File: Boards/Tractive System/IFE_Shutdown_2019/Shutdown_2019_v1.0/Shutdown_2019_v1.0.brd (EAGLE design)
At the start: 88.9 x 76.2 mm, 118 parts, among them Q1 DMN6140L-7, Q10 DMN6140L-7, Q11 DMP3099L-7, Q12 IRLML6346PBF, Q13 IRLML6346PBF, Q14 IRLML6346PBF, Q15 DMP3099L-7, Q16 DMN6140L-7, Q17 IRLML6346PBF, Q18 DMN6140L-7, Q2 DMN6140L-7, Q20 DMN6140L-7, Q21 DMN6140L-7, Q3 DMN6140L-7, Q4 DMN6140L-7, Q5 DMN6140L-7, Q6 DMP3099L-7, Q9 DMN6140L-7, U1 STM32F103CBT6, U2 STM32F103CBT6

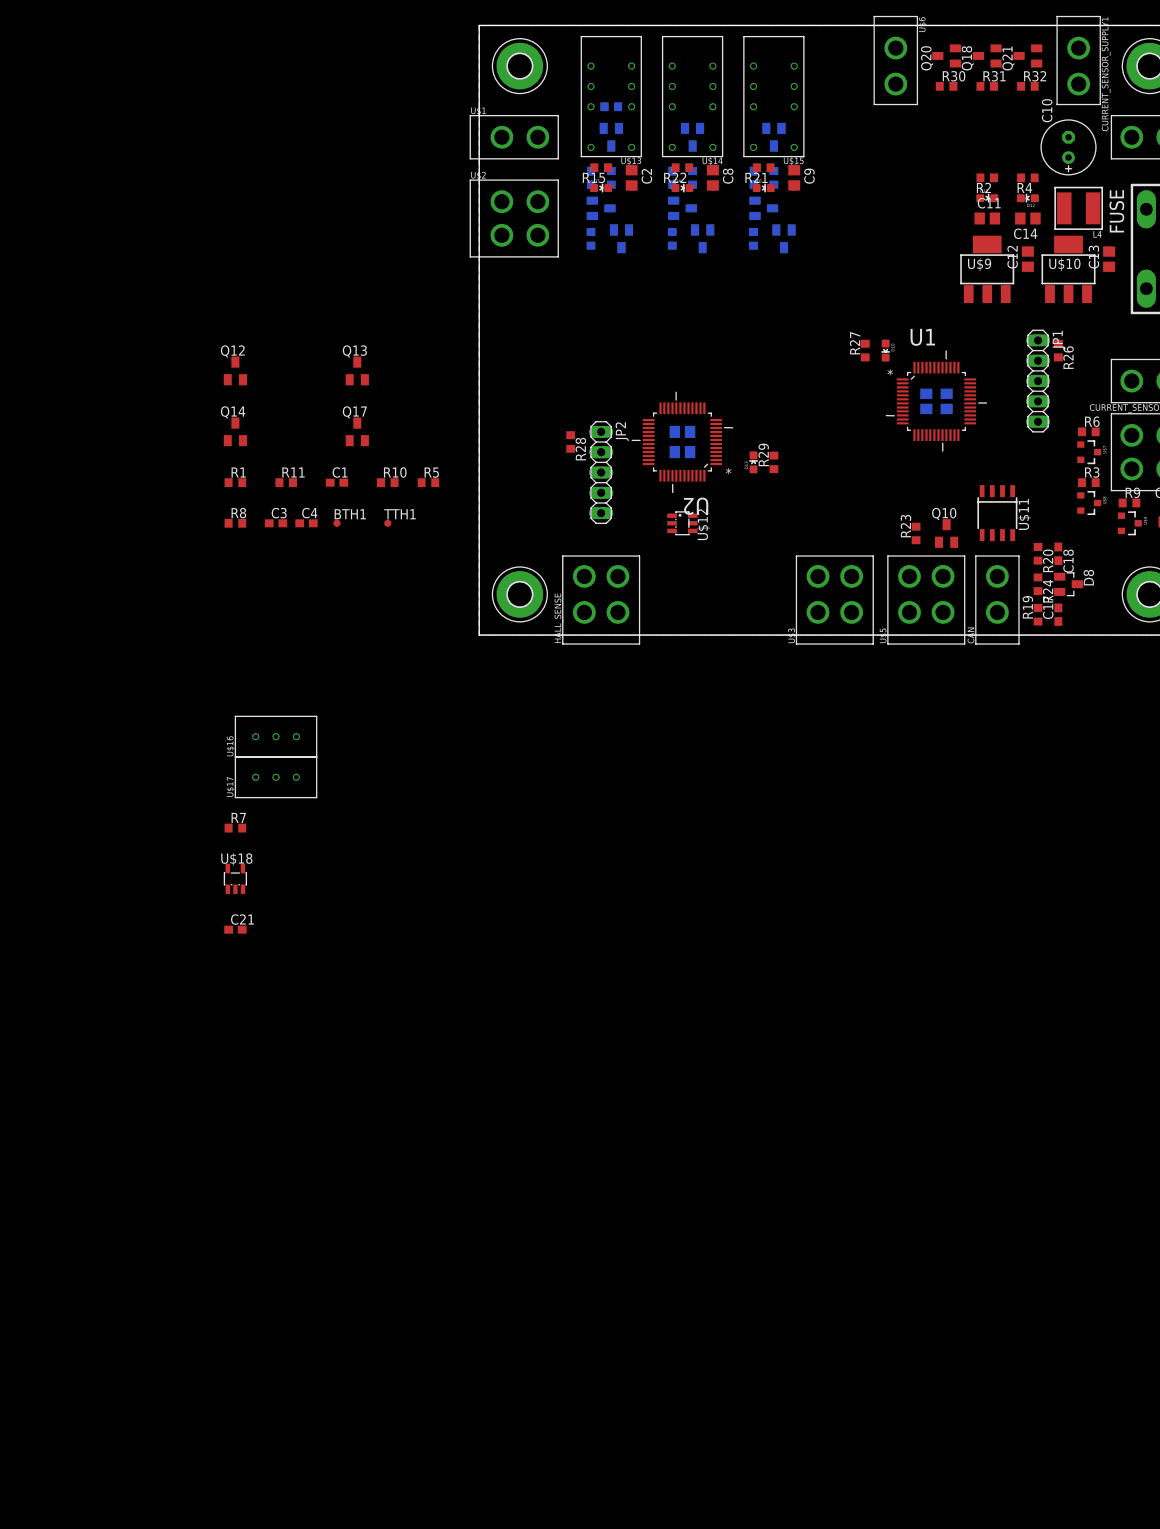
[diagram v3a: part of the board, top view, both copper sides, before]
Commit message: More work, inputs protected with zener and LPF
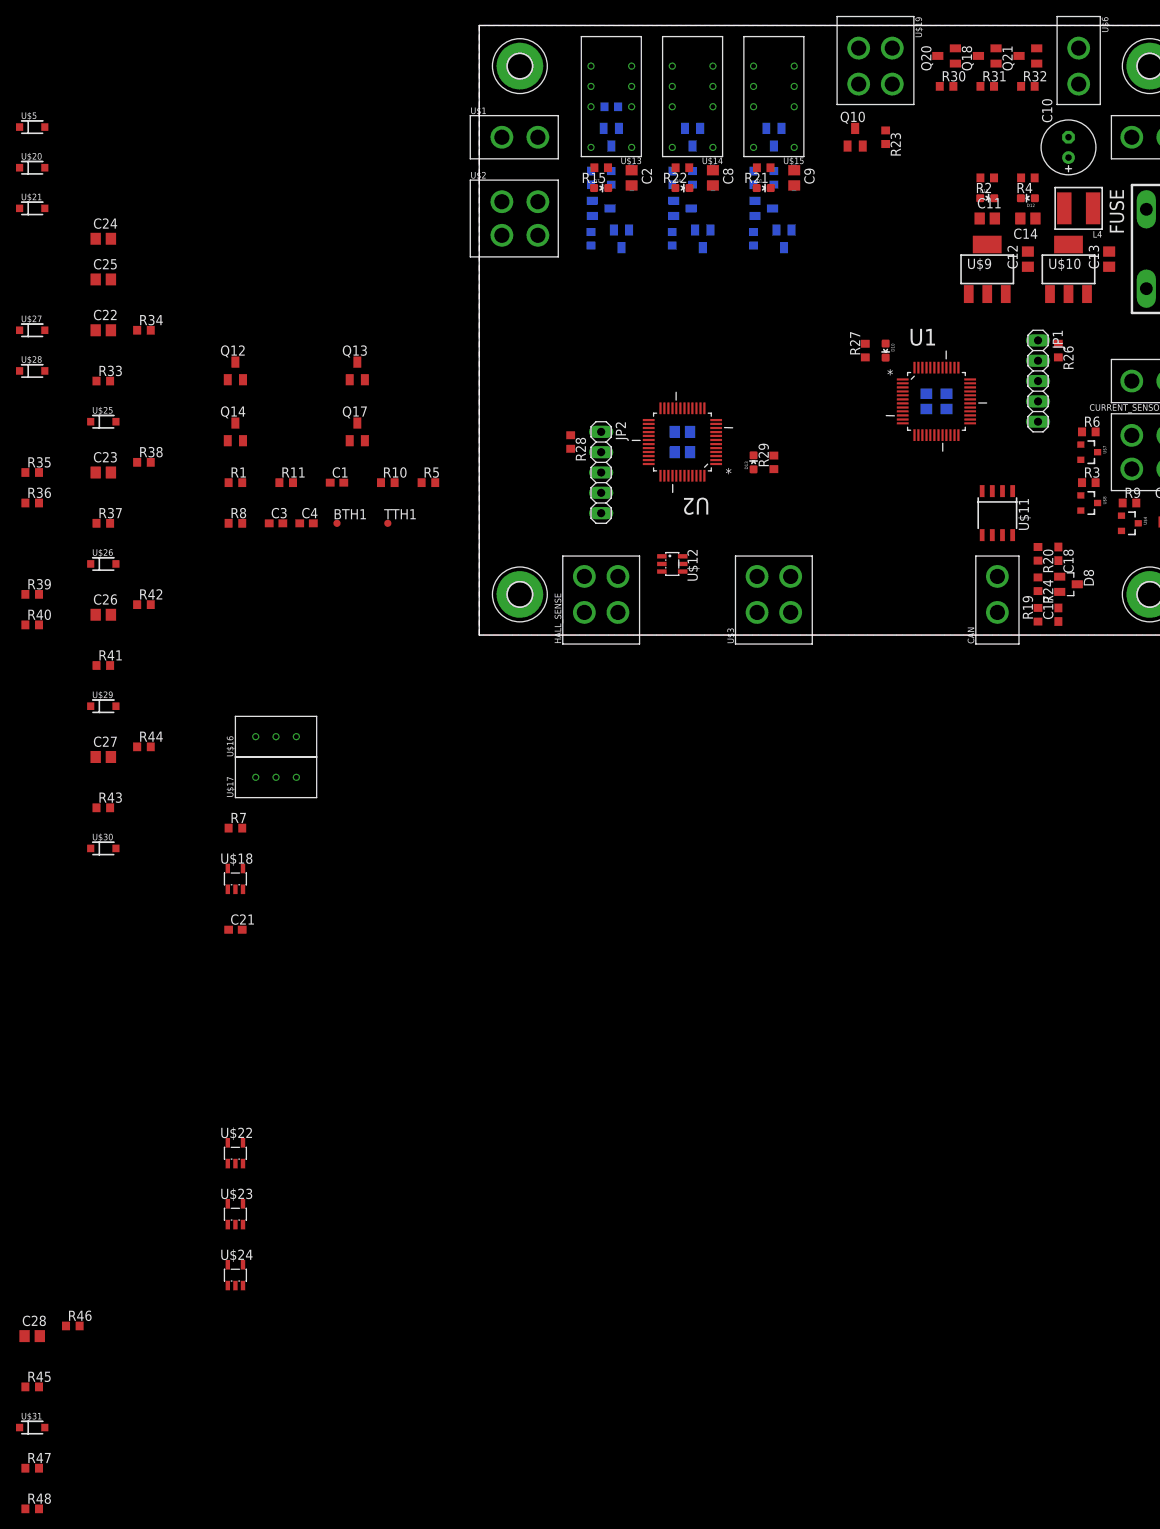
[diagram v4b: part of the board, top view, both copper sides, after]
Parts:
- removed CURRENT_SENSOR_SUPPLY1: MINIFIT_JR_5566-02, Display_Custom:MINIFIT_JR_5566-02
- added C22, C23, C24, C25, C26, C27, C28: 0.1u, rcl:C0805
- added R33, R35, R36, R37, R41, R43, R45: 100, rcl:R0603
- added R34, R38, R39, R40, R42, R44, R46: 100k, rcl:R0603
- added R47, R48: 10k, rcl:R0603
- added U$19: MINIFIT_JR_5566-04, Display_Custom:MINIFIT_JR_5566-04
- added U$20, U$21: BZT52C, DIODES_INC:SOD-123
- added U$22, U$23, U$24: LMV321L, STM:SOT23-5
- added U$25, U$26, U$28, U$29, U$30, U$31: BZT52C13, DIODES_INC:SOD-123
- added U$27: BZT52C5V6, DIODES_INC:SOD-123
- R25: value 10k -> 1k
- U$5: value MINIFIT_JR_5566-04 -> BZT52C; device Display_Custom:MINIFIT_JR_5566-04 -> DIODES_INC:SOD-123
- moved U$5 126.1 mm to (-55.9, 63.5)
- moved Q10 50.8 mm to (47.0, 62.2)
- moved R23 49.7 mm to (50.8, 62.2), turned to 270 degrees
- moved U$6 22.9 mm to (74.9, 71.1)
- moved U$3 7.62 mm to (36.8, 5.08)
- moved U$12 5.24 mm to (24.1, 8.89)
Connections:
- net N$20 renamed THROTTLE_A_F
- removed net REGEN: U$5.3
- removed net WHEEL_ANGLE: U$5.1
- new net FAULT_BMS_F: C23.1, C6.1, Q3.1, R17.2, R38.2
- new net FAULT_BSPD_F: C7.1, Q5.1, R16.2
- new net FAULT_IMD_F: C26.1, C5.1, Q16.1, R18.2, R42.2
- new net FAULT_RESET_F: C22.1, Q11.1, Q15.1, Q6.1, R25.1, R34.2
- new net N$13: R35.2, R39.1, U$27.C
- new net N$26: C24.1, R39.2
- new net N$29: R33.2, R34.1, U$25.C
- new net N$30: C28.1, R46.2
- new net N$33: R35.1
- new net N$36: R45.1
- new net N$37: R37.2, R38.1, U$26.C
- new net N$39: U$22.1
- new net N$40: U$22.3, U$22.4
- new net N$41: U$24.3, U$24.4
- new net N$45: U$24.1
- new net N$46: U$23.1
- new net N$47: U$23.3, U$23.4
- new net N$49: R41.2, R42.1, U$29.C
- new net N$50: R36.2, R40.1, U$28.C
- new net N$51: C25.1, R40.2
- new net N$54: R36.1
- new net N$55: R43.2, R44.1, U$30.C
- new net N$56: C27.1, R44.2
- new net N$57: R43.1
- net +5V: now also R47.1, R48.1, U$19.1, U$22.5, U$23.5, U$24.5; no longer CURRENT_SENSOR_SUPPLY1.1
- net FAULT_BMS: now also R37.1; no longer C6.1, Q3.1, R17.2
- net FAULT_BSPD: no longer C7.1, Q5.1, R16.2
- net FAULT_IMD: now also R41.1; no longer C5.1, Q16.1, R18.2
- net FAULT_RESET: now also R33.1, U$19.4; no longer Q11.1, Q15.1, Q6.1, R25.1, U$5.4
- net GND: now also C22.2, C23.2, C24.2, C25.2, C26.2, C27.2, C28.2, U$19.3, U$22.2, U$23.2, U$24.2, U$25.A, U$26.A, U$27.A, U$28.A, U$29.A, U$30.A, U$31.A
- net HV_CONNECTED: now also U$19.2; no longer CURRENT_SENSOR_SUPPLY1.2
- net N$22: now also R47.2
- net N$23: now also R48.2
- net N$7: now also R45.2, R46.1, U$31.C; no longer Q4.3
- net RTDS-: now also Q4.3

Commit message: Nearly complete... Just BSPD Circuit left
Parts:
- removed C28: 0.1u, rcl:C0805
- removed R46: 100k, rcl:R0603
- removed U$20, U$21, U$5: BZT52C, DIODES_INC:SOD-123
- removed U$31: BZT52C13, DIODES_INC:SOD-123
- added C29, C30, C31, C32: 0.1u, rcl:C0805
- added C33, C34, C35, C36: 0.001u, rcl:C0805
- added R49, R51, R53, R55: 100, rcl:R0603
- added R50, R52, R54, R56: 100k, rcl:R0603
- added R57, R59, R61, R63: 10, rcl:R0603
- added R58, R60, R62, R64: 10k, rcl:R0603
- added R65, R66, R67, R68: 1k, rcl:R0603
- added U$32, U$33, U$34, U$35, U$36, U$37, U$38, U$39: BZT52C5V6, DIODES_INC:SOD-123
- R45: value 100 -> 10k
- moved R45 146.1 mm to (-55.9, -240.0)
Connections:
- net N$41 renamed BRAKE_PRESSURE_F
- net N$47 renamed THROTTLE_B_F
- removed net HALL_FL_3_3: U2.25
- removed net HALL_FR_3_3: U2.26
- removed net HALL_RL_3_3: U2.27
- removed net HALL_RR_3_3: U2.28
- removed net N$18: U1.30
- removed net N$22: R47.2, U$12.4
- removed net N$23: R48.2, U$12.3
- removed net N$30: C28.1, R46.2
- removed net N$36: R45.1
- removed net N$40: U$22.3, U$22.4
- removed net N$5: U1.29
- removed net N$7: R45.2, R46.1, U$31.C
- removed net REGEN_3_3: U1.11
- new net HALL_FL_F: C33.1, R58.2, U2.25
- new net HALL_FR_F: C34.1, R60.2, U2.26
- new net HALL_RL_F: C35.1, R62.2, U2.27
- new net HALL_RR_F: C36.1, R64.2, U2.28
- new net N$20: R49.2, R50.1, U$32.C
- new net N$38: C29.1, R50.2
- new net N$52: R51.2, R52.1, U$33.C
- new net N$53: C30.1, R52.2
- new net N$59: R53.2, R54.1, U$34.C
- new net N$60: C31.1, R54.2
- new net N$62: R55.2, R56.1, U$35.C
- new net N$63: C32.1, R56.2
- new net N$64: R55.1
- new net N$65: R57.2, R58.1, R65.1, U$36.C
- new net N$68: R59.2, R60.1, R66.1, U$37.C
- new net N$71: R61.2, R62.1, R67.1, U$38.C
- new net N$74: R63.2, R64.1, R68.1, U$39.C
- net +5V: now also R45.2, R65.2, R66.2, R67.2, R68.2
- net BRAKE_PRESSURE: now also R53.1
- net GND: now also C29.2, C30.2, C31.2, C32.2, C33.2, C34.2, C35.2, C36.2, U$32.A, U$33.A, U$34.A, U$35.A, U$36.A, U$37.A, U$38.A, U$39.A; no longer C28.2, U$31.A
- net HALL_FL: now also R57.1
- net HALL_FR: now also R59.1
- net HALL_RL: now also R61.1
- net HALL_RR: now also R63.1
- net SCL_TC: now also R48.2, U$12.3
- net SDA_TC: now also R47.2, U$12.4
- net THROTTLE_A: now also R51.1
- net THROTTLE_A_F: now also U$22.3, U$22.4
- net THROTTLE_B: now also R49.1
- net THROTTLE_OUT: now also R45.1

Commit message: Moving to layout of shutdown
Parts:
- removed U$27, U$35: BZT52C5V6, DIODES_INC:SOD-123
- removed U$28, U$30: BZT52C13, DIODES_INC:SOD-123
- added BRAKE, CURR: PV36, BOURNS:PV36
- added C28: 0.1u, resistor:C0603
- added Q7: DMN6140L-7, TRANS:SOT23
- added R46, R69, R70, R71, R72, R73, R74: 10k, rcl:R0603
- added U$20, U$5: TS881, STM:SOT23-5
- added U$21: BZT52C13, DIODES_INC:SOD-123
- C24, C27: device rcl:C0805 -> resistor:C0603
- C25: value 0.1u -> 0.01u; device rcl:C0805 -> resistor:C0603
- C31: value 0.1u -> 0.001u
- R11: value 100k -> 1k
- R35: value 100 -> 1k
- R36: value 100 -> 100k; device rcl:R0603 -> resistor:R0603
- R39: value 100k -> 10k; device rcl:R0603 -> resistor:R0603
- R40, R44: value 100k -> 1k; device rcl:R0603 -> resistor:R0603
- R43: value 100 -> 10k; device rcl:R0603 -> resistor:R0603
- R49, R51, R53: value 100 -> 10
- R54: value 100k -> 10k
- U$16, U$17: value PV36 -> TS881; device BOURNS:PV36 -> STM:SOT23-5
- moved C33 273.1 mm to (-62.2, 86.4)
- moved C34 273.1 mm to (-55.9, 86.4)
- moved C35 273.1 mm to (-49.5, 86.4)
- moved C36 273.1 mm to (-62.2, 80.0)
- moved R45 273.1 mm to (-62.2, 33.0)
- moved R58 273.1 mm to (-57.1, 80.0)
- moved R60 273.1 mm to (-50.8, 80.0)
- moved R61 273.1 mm to (-62.2, 68.6)
- moved R63 273.1 mm to (-57.1, 68.6)
- moved R65 273.1 mm to (-62.2, 53.3)
- moved R66 273.1 mm to (-62.2, 48.3)
- moved R67 273.1 mm to (-62.2, 43.2)
- moved R68 273.1 mm to (-62.2, 38.1)
- moved U$36 273.1 mm to (-50.8, 68.6)
- moved U$37 273.1 mm to (-62.2, 63.5)
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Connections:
- removed net BMS_FAULT: U$2.1
- removed net BRAKE_IN: R10.1
- removed net BRAKE_PRESSURE_3_3: U1.10
- removed net CAN_SBTY: U1.31
- removed net CURRENT_IN: R8.1
- removed net FAULT_BMS_STATUS: Q2.1
- removed net FAULT_BSPD_STATUS: Q1.1
- removed net FAULT_IMD_STATUS: Q9.1
- removed net I2C1_SCL: U1.42
- removed net I2C1_SDA: U1.43
- removed net IMD_FAULT: U$2.3
- removed net N$26: C24.1, R39.2
- removed net N$33: R35.1
- removed net N$39: U$22.1
- removed net N$4: C4.1, R1.1
- removed net N$45: U$24.1
- removed net N$46: U$23.1
- removed net N$50: R36.2, R40.1, U$28.C
- removed net N$51: C25.1, R40.2
- removed net N$54: R36.1
- removed net N$55: R43.2, R44.1, U$30.C
- removed net N$56: C27.1, R44.2
- removed net N$57: R43.1
- removed net N$62: R55.2, R56.1, U$35.C
- removed net N$63: C32.1, R56.2
- removed net N$64: R55.1
- removed net THROTTLE_A_3_3: U1.18
- removed net THROTTLE_B_3_3: U1.19
- removed net THROTTLE_TH: TTH1.TP, U$17.W
- removed net VDDA: U1.9
- new net BRAKE_PRESSURE_F_3_3: R70.1, R71.2, U1.10
- new net BSPD_BRAKE_COND: C3.1, Q13.1, R1.1
- new net BSPD_CURR_COND: C4.1, Q12.1, R36.1
- new net BSPD_OC: Q17.1, U$17.1
- new net BSPD_SC: Q14.1, U$16.1
- new net CURRENT_SENSE_F: C25.1, R44.1, U$16.4, U$17.3, U$20.3
- new net CURR_TH: CURR.W, TTH1.TP, U$20.4
- new net N$18: R1.2, U$5.1
- new net OC_TH: R11.1, R43.2, U$17.4
- new net PRECHARGE_COMPLETE_3_3: Q7.3, R74.1, U1.42
- new net PRECHARGE_COMP_F: C32.1, Q7.1, R56.2
- new net SC_TH: R39.1, R40.2, U$16.3
- new net THROTTLE_A_F_3_3: R69.1, R73.2, U1.18
- new net THROTTLE_B_F_3_3: R46.1, R72.2, U1.19
- net +3V3: now also R74.2, U1.9
- net +5V: now also BRAKE.A, C24.1, C27.1, C28.1, CURR.A, R35.2, R39.2, U$16.5, U$17.5, U$20.5, U$5.5; no longer R1.2, U$16.A, U$17.A
- net BRAKE_PRESSURE_F: now also R10.1, R70.2, U$5.3
- net BRAKE_TH: now also BRAKE.W, U$5.4; no longer U$16.W
- net CAN_STBY: now also U1.31
- net CURRENT_SENSE: now also R44.2, R8.1
- net FAULT_BMS: now also U$2.1
- net FAULT_BMS_STAT: now also Q2.1
- net FAULT_BSPD_STAT: now also Q1.1
- net FAULT_IMD: now also U$2.3
- net FAULT_IMD_STAT: now also Q9.1
- net GND: now also BRAKE.B, C28.2, CURR.B, Q7.2, R40.1, R43.1, R71.1, R72.1, R73.1, U$16.2, U$17.2, U$20.2, U$21.A, U$5.2; no longer U$16.B, U$17.B, U$27.A, U$28.A, U$30.A, U$35.A
- net N$13: now also R36.2, U$20.1; no longer R35.2, R39.1, U$27.C
- net N$2: now also R55.2, R56.1, U$21.C; no longer C3.1, R11.1
- net N$38: now also U$22.1
- net N$53: now also U$23.1
- net N$59: now also R35.1
- net N$60: now also U$24.1
- net PRECHARGE_COMPLETE: now also R55.1
- net THROTTLE_A_F: now also R69.2
- net THROTTLE_B_F: now also R46.2
